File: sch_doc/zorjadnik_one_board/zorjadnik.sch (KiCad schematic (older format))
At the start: 50 parts, among them J1 OUT1, J10 output GND, J11 power supply GND, J12 spare port, J2 OUT2, J3 Vsb, J4 GND, J6 firmware, J7 cooling fan, J9 power supply Vout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

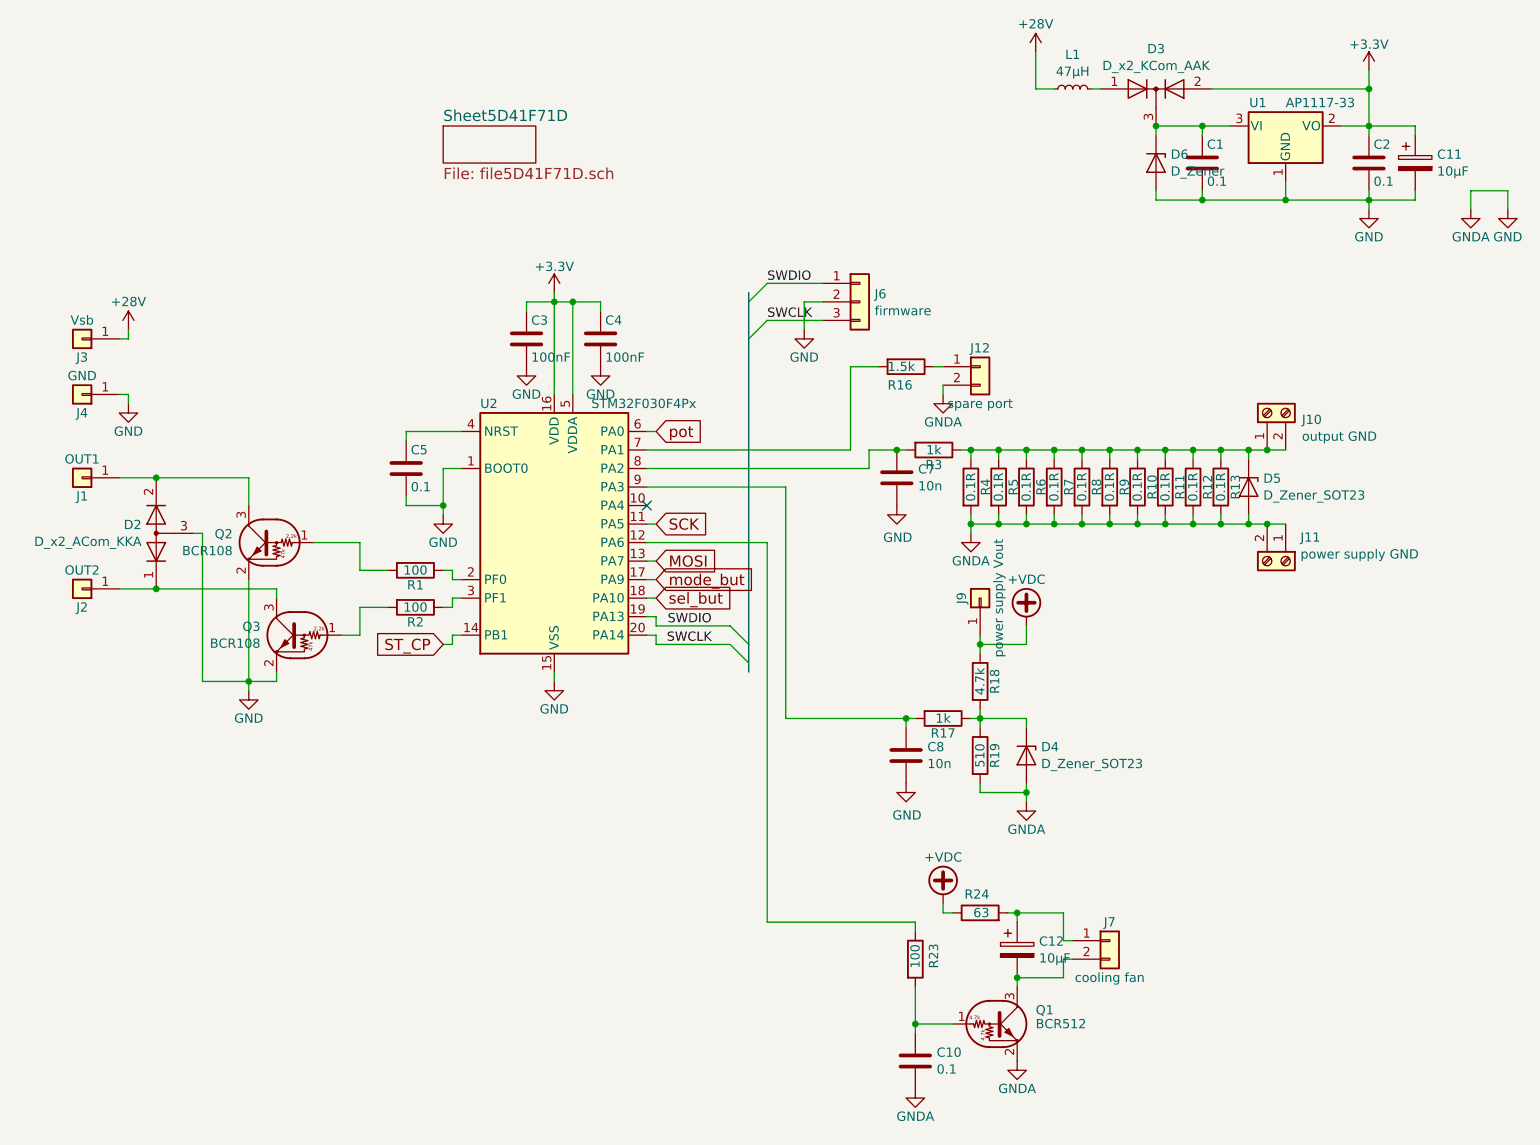
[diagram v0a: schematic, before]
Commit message: список компонентов
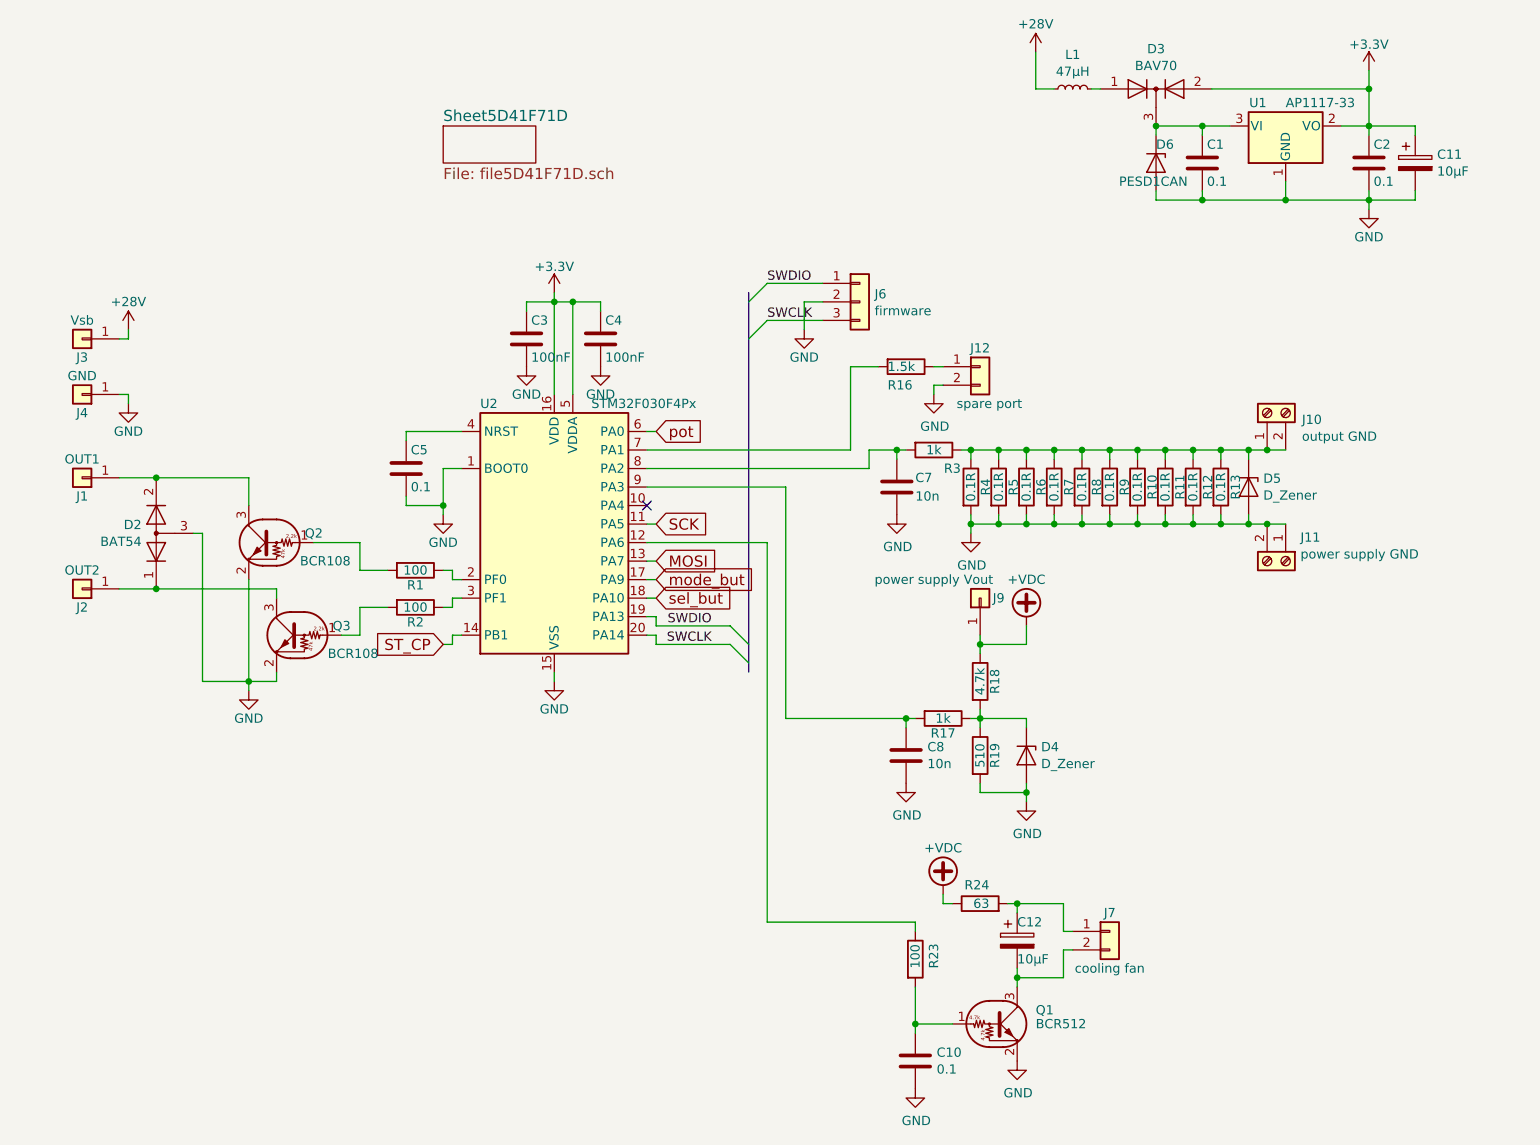
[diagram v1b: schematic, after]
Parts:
- D2: value D_x2_ACom_KKA -> BAT54
- D3: value D_x2_KCom_AAK -> BAV70
- D4, D5: value D_Zener_SOT23 -> D_Zener
- D6: value D_Zener -> PESD1CAN
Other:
- moved on the sheet: C12, C7, J7, R24

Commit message: убрал сохранение настроек, не умею в такое
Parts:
- C1, C2, C3, C4, C5: symbol zorjadnik-rescue:C-zorjadnik-rescue -> zorjadnik:C-zorjadnik
- C10, C7, C8: symbol zorjadnik-rescue:C-Device1 -> zorjadnik:C-Device1
- C11, C12: symbol zorjadnik-rescue:CP-Device1 -> zorjadnik:CP-Device1
- D2: symbol zorjadnik-rescue:D_x2_ACom_KKA-Device1 -> zorjadnik:D_x2_ACom_KKA-Device1
- D3: symbol zorjadnik-rescue:D_x2_KCom_AAK-Device1 -> zorjadnik:D_x2_KCom_AAK-Device1
- D6: symbol zorjadnik-rescue:D_Zener-Device1 -> zorjadnik:D_Zener-Device1
- J1, J2, J3, J4, J9: symbol zorjadnik-rescue:Conn_01x01-Connector_Generic1 -> zorjadnik:Conn_01x01-Connector_Generic1
- J10, J11: symbol zorjadnik-rescue:Screw_Terminal_01x02-Connector1 -> zorjadnik:Screw_Terminal_01x02-Connector1
- J12, J7: symbol zorjadnik-rescue:Conn_01x02-Connector_Generic1 -> zorjadnik:Conn_01x02-Connector_Generic1
- J6: symbol zorjadnik-rescue:Conn_01x03-Connector_Generic1 -> zorjadnik:Conn_01x03-Connector_Generic1
- L1: symbol zorjadnik-rescue:L_Small-Device1 -> zorjadnik:L_Small-Device1
- R1, R10, R11, R12, R13, R17, R18, R19, R2, R3, R4, R5, R6, R7, R8, R9: symbol zorjadnik-rescue:R-zorjadnik-rescue -> zorjadnik:R-zorjadnik
- R16, R23, R24: symbol zorjadnik-rescue:R-Device1 -> zorjadnik:R-Device1
- U1: symbol zorjadnik-rescue:AP1117-33-zorjadnik-rescue -> zorjadnik:AP1117-33-zorjadnik
- U2: symbol zorjadnik-rescue:STM32F030F4Px-MCU_ST_STM32F01 -> zorjadnik:STM32F030F4Px-MCU_ST_STM32F01
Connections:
- net GND: no longer J11.1 (Pin_1)
- net at D5.3 (K), J10.1 (Pin_1), R10.1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: no longer J10.2 (Pin_2)
- net at J2.1 (Pin_1), Q3.3 (C): no longer D2.1 (K)
- net at J1.1 (Pin_1), Q2.3 (C): no longer D2.2 (K)
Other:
- moved on the sheet: C1, C10, C11, C12, C2, C3, C4, C5, C7, C8, D2, D3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

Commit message: добавил сохрааниение настроек, подправил переменник, не проверял
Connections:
- net at U2.12 (PA6): now also R23.2; no longer R23.1
- net at C10.1, Q1.1 (B): now also R23.1; no longer R23.2
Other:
- moved on the sheet: C10, C12, C7, C8, D4, D5, J10, J11, J12, J7, J9, Q1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

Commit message: наладил, как сделаю трансформатор, так будет релиз
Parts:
- removed R10, R11, R12, R13, R9: 0.1R, Resistor_SMD:R_2010_5025Metric, symbol zorjadnik:R-zorjadnik
- added R14, R15: 1k, Resistor_SMD:R_0805_2012Metric, symbol device:R
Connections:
- net +3V3: now also R14.2, R15.2
- net GND: now also J11.1 (Pin_1)
- net at R1.1, U2.2 (PF0): now also R14.1
- net at R2.1, U2.3 (PF1): now also R15.1
- net at D5.3 (K), J10.1 (Pin_1), R3.1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: now also J10.2 (Pin_2)
- net at J2.1 (Pin_1), Q3.3 (C): now also D2.1 (K)
- net at J1.1 (Pin_1), Q2.3 (C): now also D2.2 (K)
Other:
- moved on the sheet: C1, C10, C11, C12, C2, C3, C4, C5, C7, C8, D2, D3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
